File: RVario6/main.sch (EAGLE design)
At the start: 7 parts, among them J1 ZX62-B-5PA, U1 32U4

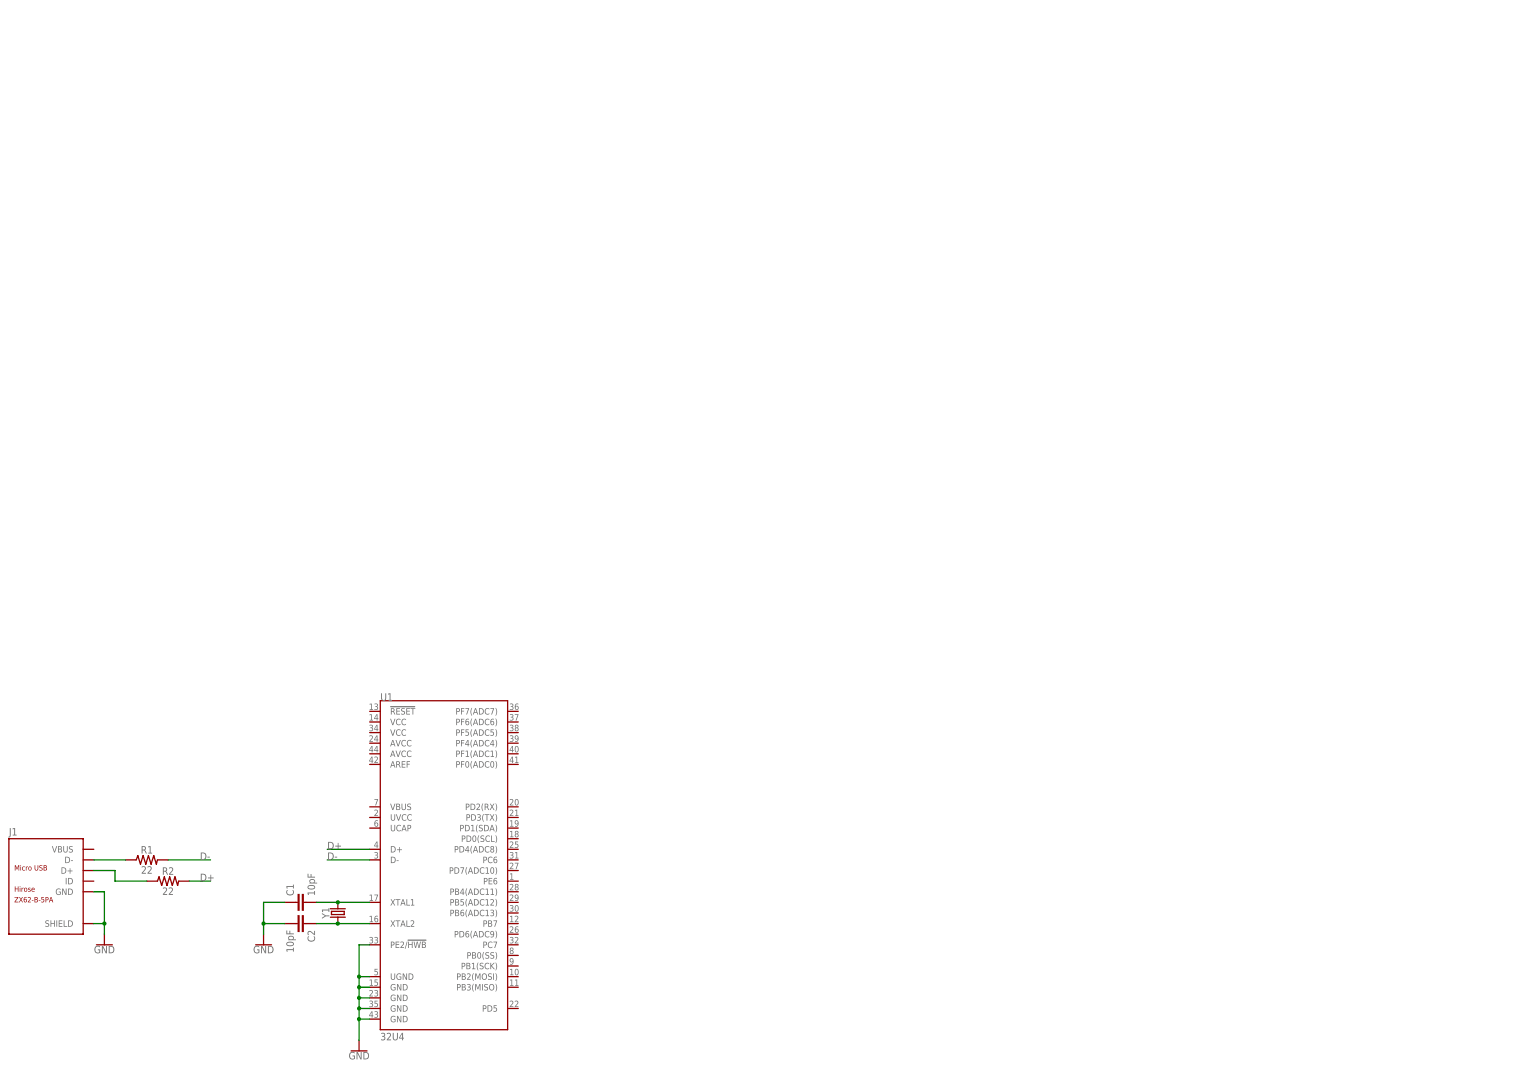
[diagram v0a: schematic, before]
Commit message: Finished schematic RVario6
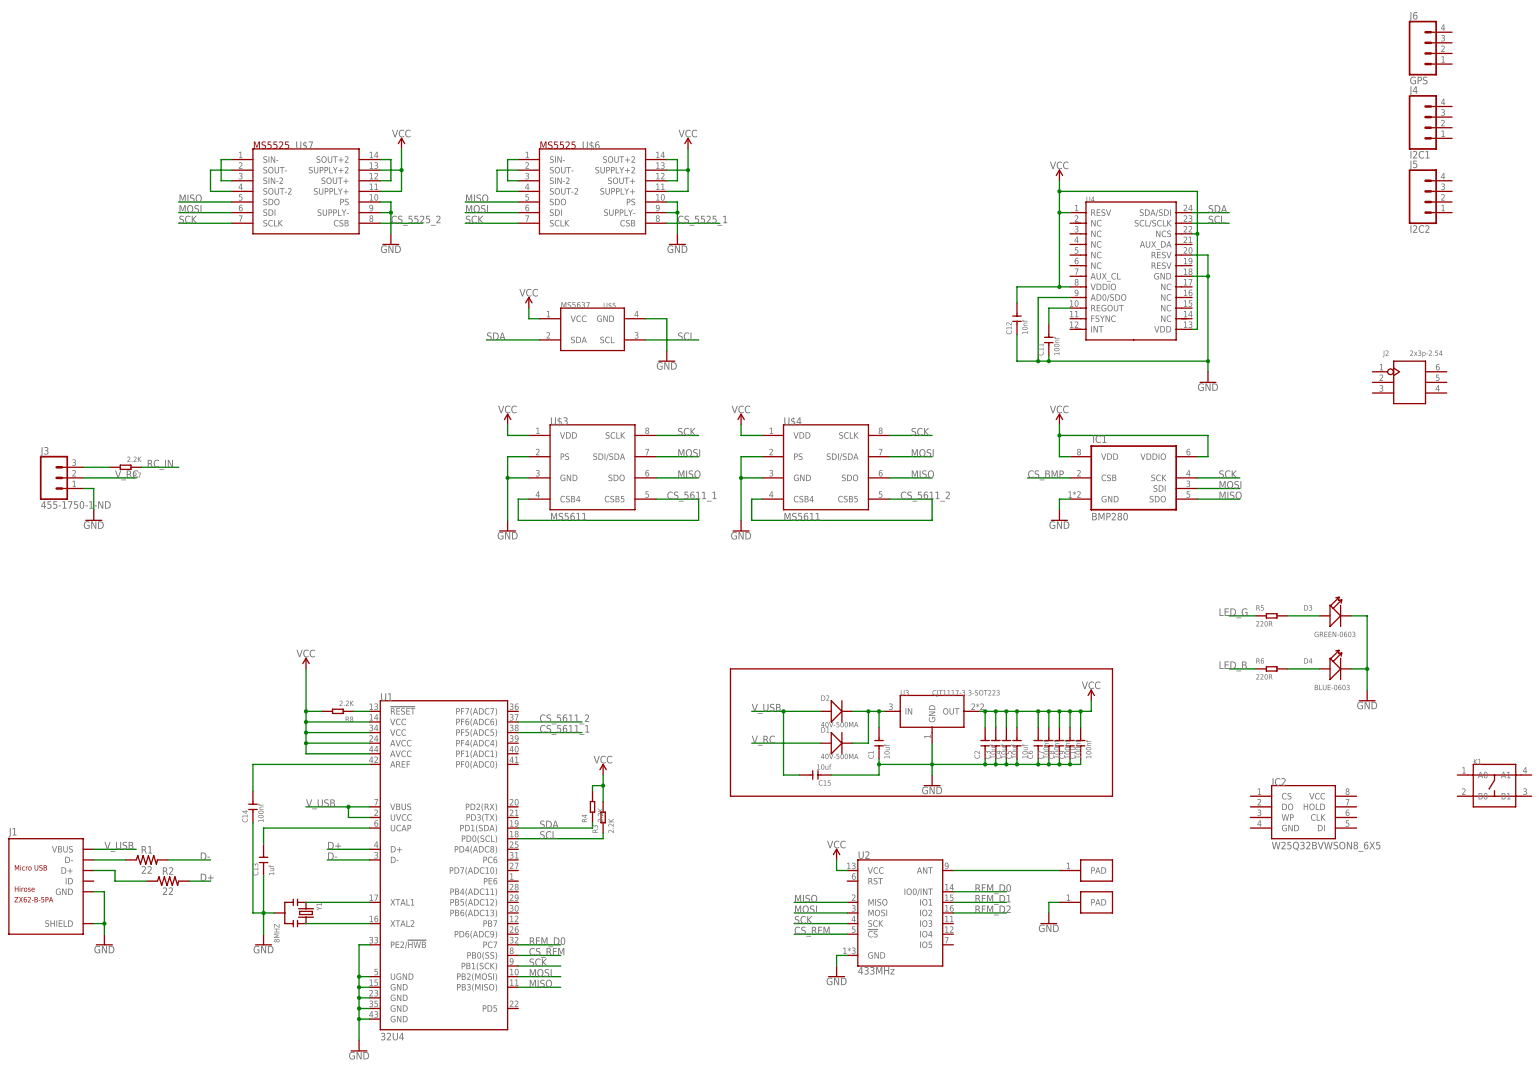
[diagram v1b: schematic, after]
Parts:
- added C10, C11, C14, C6, C7, C8, C9: 100nf, Seeed-Capacitor:CERAMIC-100NF-50V-10%-X7R(0603)
- added C12: 10nf, Seeed-Capacitor:CERAMIC-10NF-50V-10%-X7R(0603)
- added C13: 1uf, Seeed-Capacitor:CERAMIC-1UF-25V-10%-X7R(0603)
- added C15, C3, C4, C5: 10uf, Seeed-Capacitor:CERAMIC-10UF-25V-10%-X5R(0805)
- added D1, D2: 40V-500MA, Seeed-Diode:SMD-DIODE-SCHOTTKY-40V-500MA(SOD-123)
- added D3: GREEN-0603, Seeed-LED:SMD-LED-CLEAR-GREEN(0603)
- added D4: BLUE-0603, Seeed-LED:SMD-LED-CLEAR-BLUE(0603)
- added IC1: BMP280, bosch-bmp280:BMP280
- added IC2: W25Q32BVWSON8_6X5, Custom_old:W25Q32BVWSON8_6X5
- added J2: 2x3p-2.54, Seeed-Connector:DIP-BLACK-MALE-HEADER(2X3P-2.54）-2.54
- added J3: 455-1750-1-ND, SparkFun-Connectors:CONN_03
- added J4: I2C1, SparkFun-Connectors:CONN_04
- added J5: I2C2, SparkFun-Connectors:CONN_04
- added J6: GPS, SparkFun-Connectors:CONN_04
- added K1: (no value), Seeed-Switch:SMD-SWITCH-TACTILE-SPST-NO(4P-D6.0MM)
- added R3, R4, R7, R8: 2.2K, Seeed-Resistor:SMD-RES-2.2K-5%-1/10W(0603)
- added R5, R6: 220R, Seeed-Resistor:SMD-RES-220R-5%-1/10W(0603)
- added U$1, U$2: PADPAD_2.5X1.5, Custom_old:PADPAD_2.5X1.5
- added U$3, U$4: MS5611, Custom_old:MS5611
- added U$5: MS5637, Custom_old:MS5637
- added U$6, U$7: MS5525, Custom_old:MS5525
- added U2: 433MHz, SparkFun-RF:RFM69HCW-433
- added U3: CJT1117-3.3-SOT223, Seeed-IC:PMIC-CJT1117-3.3(SOT223)
- added U4: (no value), Seeed-Sensor:MOTION/POSITION-MPU-9250(QFN24G)
- C1, C2: value 10pF -> 10uf; device SparkFun-Capacitors:0.1UF-0603-25V-5% -> Seeed-Capacitor:CERAMIC-10UF-25V-10%-X5R(0805)
- Y1: value (none) -> 8MHZ; device SparkFun-Clocks:CRYSTALSMD-5X3.2-4PAD -> Seeed-Crystal Oscillator:SMD-CRYSTAL-8MHZ--0.3%-150R(3P-3.6X1.3MM)
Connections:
- new net CS_5525_1: U$6.CSB
- new net CS_5525_2: U$7.CSB
- new net CS_5611_1: U$3.CSB4, U$3.CSB5, U1.PF5(ADC5)
- new net CS_5611_2: U$4.CSB4, U$4.CSB5, U1.PF6(ADC6)
- new net CS_BMP: IC1.CSB
- new net CS_RFM: U1.PB0(SS), U2.!CS
- new net LED_B: R6.1
- new net LED_G: R5.1
- new net MISO: IC1.SDO, U$3.SDO, U$4.SDO, U$6.SDO, U$7.SDO, U1.PB3(MISO), U2.MISO
- new net MOSI: IC1.SDI, U$3.SDI/SDA, U$4.SDI/SDA, U$6.SDI, U$7.SDI, U1.PB2(MOSI), U2.MOSI
- new net N$10: C11.2, U4.REGOUT
- new net N$11: U$7.SIN-, U$7.SIN-2
- new net N$12: U$7.SOUT-, U$7.SOUT-2
- new net N$13: U$7.SOUT+, U$7.SOUT+2
- new net N$14: D3.+, R5.2
- new net N$15: D4.+, R6.2
- new net N$16: C13.2, U1.UCAP
- new net N$17: J3.3, R7.2
- new net N$18: R8.1, U1.!RESET
- new net N$19: C14.2, U1.AREF
- new net N$5: C1.2, D1.-, D2.-, U3.IN
- new net N$6: U$2.PAD, U2.ANT
- new net N$7: U$6.SIN-, U$6.SIN-2
- new net N$8: U$6.SOUT-, U$6.SOUT-2
- new net N$9: U$6.SOUT+, U$6.SOUT+2
- new net RC_IN: R7.1
- new net RFM_D0: U1.PC7, U2.IO0/INT
- new net RFM_D1: U2.IO1
- new net RFM_D2: U2.IO2
- new net SCK: IC1.SCK, U$3.SCLK, U$4.SCLK, U$6.SCLK, U$7.SCLK, U1.PB1(SCK), U2.SCK
- new net SCL: R3.1, U$5.SCL, U1.PD0(SCL), U4.SCL/SCLK
- new net SDA: R4.1, U$5.SDA, U1.PD1(SDA), U4.SDA/SDI
- new net VCC: C10.2, C12.2, C2.2, C3.2, C4.2, C5.2, C6.2, C7.2, C8.2, C9.2, IC1.VDD, IC1.VDDIO, R3.2, R4.2, R8.2, U$3.VDD, U$4.VDD, U$5.VCC, U$6.SUPPLY+, U$6.SUPPLY+2, U$7.SUPPLY+, U$7.SUPPLY+2, U1.AVCC@24, U1.AVCC@44, U1.VCC@14, U1.VCC@34, U2.VCC, U3.OUT, U4.NCS, U4.RESV, U4.VDD, U4.VDDIO
- new net V_RC: D1.+, J3.2
- new net V_USB: C15.2, D2.+, J1.VBUS, U1.UVCC, U1.VBUS
- net GND: now also C10.1, C11.1, C12.1, C13.1, C14.1, C15.1, C2.1, C3.1, C4.1, C5.1, C6.1, C7.1, C8.1, C9.1, D3.-, D4.-, IC1.GND, J3.1, U$1.PAD, U$3.GND, U$3.PS, U$4.GND, U$4.PS, U$5.GND, U$6.PS, U$6.SUPPLY-, U$7.PS, U$7.SUPPLY-, U2.GND, U3.GND, U4.AD0/SDO, U4.GND, U4.RESV@2, Y1.2; no longer C2.2
- net N$1: now also Y1.1; no longer C1.2, Y1.2
- net N$2: now also Y1.3; no longer C2.1, Y1.1

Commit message: Rvario6 updates
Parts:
- added J7: MICROSD-9P, Seeed-Connector:MICRO-SD-CARD-HOLDER-9P
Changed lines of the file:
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@@
 <part name="J6" library="SparkFun-Connectors" deviceset="CONN_04" device="" value="GPS"/>
 <part name="K1" library="Seeed-Switch" deviceset="SMD-SWITCH-TACTILE-SPST-NO(4P-D6.0MM)" device=""/>
+<part name="J7" library="Seeed-Connector" deviceset="MICRO-SD-CARD-HOLDER-9P" device="" value="MICROSD-9P"/>
 </parts>
 <sheets>
@@
 <instance part="J6" gate="G$1" x="342.9" y="269.24"/>
 <instance part="K1" gate="G$1" x="358.14" y="93.98"/>
+<instance part="J7" gate="G$1" x="391.16" y="157.48"/>
 </instances>
 <busses>

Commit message: Partiall routed
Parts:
- removed J5: I2C2, SparkFun-Connectors:CONN_04
- added C16, C17, C18: 100nf, Seeed-Capacitor:CERAMIC-100NF-50V-10%-X7R(0603)
- J4: value I2C1 -> GPS
- J6: value GPS -> I2C
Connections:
- net N$6 renamed ANT
- removed net N$18: R8.1, U1.!RESET
- new net BTN: K1.A0, U1.PD4(ADC8)
- new net CS_FLASH: IC2.CS, U1.PF7(ADC7)
- new net CS_SD: J7.CS, U1.PF4(ADC4)
- new net MRST: J4.2, U1.PD2(RX)
- new net MTSR: J4.1, U1.PD3(TX)
- new net RESET: J2.3, R8.1, U1.!RESET
- net CS_5525_1: now also U1.PC6
- net CS_5525_2: now also U1.PD7(ADC10)
- net CS_BMP: now also U1.PE6
- net GND: now also C16.1, C17.1, C18.1, IC2.GND, J2.4, J4.3, J6.1, J7.G1, J7.G2, J7.G3, J7.G4, J7.VSS, K1.B0, K1.B1
- net LED_B: now also U1.PF0(ADC0)
- net LED_G: now also U1.PF1(ADC1)
- net MISO: now also IC2.DO, J2.1, J7.DO
- net MOSI: now also IC2.DI, J2.5, J7.DI
- net RC_IN: now also U1.PB4(ADC11)
- net RFM_D1: now also U1.PB5(ADC12)
- net RFM_D2: now also U1.PB6(ADC13)
- net SCK: now also IC2.CLK, J2.2, J7.SCLK
- net SCL: now also J6.4
- net SDA: now also J6.3
- net VCC: now also C16.2, C17.2, C18.2, IC2.HOLD, IC2.VCC, IC2.WP, J2.6, J4.4, J6.2, J7.VDD
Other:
- moved on the sheet: IC2, J4, R8

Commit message: partially routed
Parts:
- removed J4: GPS, SparkFun-Connectors:CONN_04
- removed R7: 2.2K, Seeed-Resistor:SMD-RES-2.2K-5%-1/10W(0603)
- added Q1, Q2: CJ2302, Seeed-Transistor:SMD-MOSFET-N-CH-20V-2.1A-CJ2302(SOT-23)
- added R10, R9: 2.2K, Seeed-Resistor:SMD-RES-2.2K-5%-1/10W(0603)
- added R11: 47K, Seeed-Resistor:SMD-RES-47K-5%-1/10W(0603)
- J3: value 455-1750-1-ND -> (none)
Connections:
- removed net MRST: J4.2, U1.PD2(RX)
- removed net MTSR: J4.1, U1.PD3(TX)
- removed net N$17: J3.3, R7.2
- new net N$6: Q2.D, R10.1
- new net RX_INV: Q1.D, R9.1, U1.PD2(RX)
- new net TX_INV: Q2.G, U1.PD3(TX)
- net CS_BMP: now also U1.PF1(ADC1); no longer U1.PE6
- net GND: now also Q1.S, Q2.S; no longer J4.3
- net LED_G: now also U1.PE6; no longer U1.PF1(ADC1)
- net RC_IN: now also J3.3, Q1.G, R10.2, R11.1; no longer R7.1, U1.PB4(ADC11)
- net VCC: now also R11.2, R9.2; no longer J4.4
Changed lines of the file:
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@@
 <part name="GND14" library="SparkFun-PowerSymbols" deviceset="GND" device=""/>
 <part name="J2" library="Seeed-Connector" deviceset="DIP-BLACK-MALE-HEADER(2X3P-2.54）" device="-2.54" value="2x3p-2.54"/>
-<part name="J3" library="SparkFun-Connectors" deviceset="CONN_03" device="" value="455-1750-1-ND"/>
-<part name="GND15" library="SparkFun-PowerSymbols" deviceset="GND" device=""/>
-<part name="R7" library="Seeed-Resistor" deviceset="SMD-RES-2.2K-5%-1/10W(0603)" device="" value="2.2K"/>
+<part name="J3" library="SparkFun-Connectors" deviceset="CONN_03" device=""/>
 <part name="IC2" library="Custom_old" deviceset="W25Q32BV" device="WSON8_6X5" package3d_urn="urn:adsk.eagle:package:8074834/1" value=""/>
 <part name="C13" library="Seeed-Capacitor" deviceset="CERAMIC-1UF-25V-10%-X7R(0603)" device="" value="1uf"/>
@@
 <part name="SUPPLY14" library="SparkFun-PowerSymbols" deviceset="VCC" device=""/>
 <part name="GND19" library="SparkFun-PowerSymbols" deviceset="GND" device=""/>
-<part name="J4" library="SparkFun-Connectors" deviceset="CONN_04" device="" value="GPS"/>
 <part name="GND20" library="SparkFun-PowerSymbols" deviceset="GND" device=""/>
 <part name="SUPPLY15" library="SparkFun-PowerSymbols" deviceset="VCC" device=""/>
-<part name="GND21" library="SparkFun-PowerSymbols" deviceset="GND" device=""/>
-<part name="SUPPLY17" library="SparkFun-PowerSymbols" deviceset="VCC" device=""/>
 <part name="C16" library="Seeed-Capacitor" deviceset="CERAMIC-100NF-50V-10%-X7R(0603)" device="" value="100nf"/>
 <part name="C17" library="Seeed-Capacitor" deviceset="CERAMIC-100NF-50V-10%-X7R(0603)" device="" value="100nf"/>
 <part name="C18" library="Seeed-Capacitor" deviceset="CERAMIC-100NF-50V-10%-X7R(0603)" device="" value="100nf"/>
+<part name="Q1" library="Seeed-Transistor" deviceset="SMD-MOSFET-N-CH-20V-2.1A-CJ2302(SOT-23)" device="" value="CJ2302"/>
+<part name="Q2" library="Seeed-Transistor" deviceset="SMD-MOSFET-N-CH-20V-2.1A-CJ2302(SOT-23)" device="" value="CJ2302"/>
+<part name="R9" library="Seeed-Resistor" deviceset="SMD-RES-2.2K-5%-1/10W(0603)" device="" value="2.2K"/>
+<part name="R10" library="Seeed-Resistor" deviceset="SMD-RES-2.2K-5%-1/10W(0603)" device="" value="2.2K"/>
+<part name="R11" library="Seeed-Resistor" deviceset="SMD-RES-47K-5%-1/10W(0603)" device="" value="47K"/>
+<part name="SUPPLY16" library="SparkFun-PowerSymbols" deviceset="VCC" device=""/>
+<part name="GND22" library="SparkFun-PowerSymbols" deviceset="GND" device=""/>
 </parts>
 <sheets>
@@
 <instance part="J2" gate="J" x="337.82" y="190.5"/>
 <instance part="J3" gate="J$1" x="12.7" y="167.64"/>
-<instance part="GND15" gate="1" x="22.86" y="157.48"/>
-<instance part="R7" gate="G$1" x="30.48" y="170.18" rot="R180"/>
 <instance part="IC2" gate="G$1" x="312.42" y="66.04"/>
 <instance part="C13" gate="G$1" x="63.5" y="76.2" rot="R90"/>
@@
 <instance part="SUPPLY14" gate="G$1" x="347.98" y="195.58"/>
 <instance part="GND19" gate="1" x="347.98" y="182.88"/>
-<instance part="J4" gate="G$1" x="342.9" y="236.22"/>
 <instance part="GND20" gate="1" x="350.52" y="261.62"/>
 <instance part="SUPPLY15" gate="G$1" x="350.52" y="276.86"/>
-<instance part="GND21" gate="1" x="350.52" y="228.6"/>
-<instance part="SUPPLY17" gate="G$1" x="350.52" y="243.84"/>
 <instance part="C16" gate="G$1" x="261.62" y="104.14" rot="R90"/>
 <instance part="C17" gate="G$1" x="264.16" y="104.14" rot="R90"/>
 <instance part="C18" gate="G$1" x="266.7" y="104.14" rot="R90"/>
+<instance part="Q1" gate="G$1" x="53.34" y="170.18"/>
+<instance part="Q2" gate="G$1" x="45.72" y="154.94"/>
+<instance part="R9" gate="G$1" x="53.34" y="182.88" rot="R90"/>
+<instance part="R10" gate="G$1" x="45.72" y="165.1" rot="R90"/>
+<instance part="R11" gate="G$1" x="45.72" y="182.88" rot="R90"/>
+<instance part="SUPPLY16" gate="G$1" x="53.34" y="190.5"/>
+<instance part="GND22" gate="1" x="45.72" y="144.78"/>
 </instances>
 <busses>
@@
 </segment>
 <segment>
-<pinref part="J3" gate="J$1" pin="1"/>
-<pinref part="GND15" gate="1" pin="GND"/>
-<wire x1="20.32" y1="165.1" x2="22.86" y2="165.1" width="0.1524" layer="91"/>
-<wire x1="22.86" y1="165.1" x2="22.86" y2="160.02" width="0.1524" layer="91"/>
-</segment>
-<segment>
 <pinref part="K1" gate="G$1" pin="B1"/>
 <pinref part="GND16" gate="1" pin="GND"/>
@@
 </segment>
 <segment>
-<pinref part="J4" gate="G$1" pin="3"/>
-<pinref part="GND21" gate="1" pin="GND"/>
-<wire x1="347.98" y1="238.76" x2="350.52" y2="238.76" width="0.1524" layer="91"/>
-<wire x1="350.52" y1="238.76" x2="350.52" y2="231.14" width="0.1524" layer="91"/>
+<pinref part="J3" gate="J$1" pin="1"/>
+<wire x1="20.32" y1="165.1" x2="30.48" y2="165.1" width="0.1524" layer="91"/>
+<wire x1="30.48" y1="165.1" x2="30.48" y2="149.86" width="0.1524" layer="91"/>
+<pinref part="Q2" gate="G$1" pin="S"/>
+<wire x1="30.48" y1="149.86" x2="45.72" y2="149.86" width="0.1524" layer="91"/>
+<pinref part="GND22" gate="1" pin="GND"/>
+<wire x1="45.72" y1="147.32" x2="45.72" y2="149.86" width="0.1524" layer="91"/>
+<junction x="45.72" y="149.86"/>
+<pinref part="Q1" gate="G$1" pin="S"/>
+<wire x1="45.72" y1="149.86" x2="53.34" y2="149.86" width="0.1524" layer="91"/>
+<wire x1="53.34" y1="149.86" x2="53.34" y2="165.1" width="0.1524" layer="91"/>
 </segment>
 </net>
@@
 </segment>
 <segment>
-<pinref part="J4" gate="G$1" pin="4"/>
-<pinref part="SUPPLY17" gate="G$1" pin="VCC"/>
-<wire x1="347.98" y1="241.3" x2="350.52" y2="241.3" width="0.1524" layer="91"/>
-<wire x1="350.52" y1="241.3" x2="350.52" y2="243.84" width="0.1524" layer="91"/>
+<pinref part="R9" gate="G$1" pin="2"/>
+<pinref part="SUPPLY16" gate="G$1" pin="VCC"/>
+<wire x1="53.34" y1="186.69" x2="53.34" y2="187.96" width="0.1524" layer="91"/>
+<pinref part="R11" gate="G$1" pin="2"/>
+<wire x1="53.34" y1="187.96" x2="53.34" y2="190.5" width="0.1524" layer="91"/>
+<wire x1="45.72" y1="186.69" x2="45.72" y2="187.96" width="0.1524" layer="91"/>
+<wire x1="45.72" y1="187.96" x2="53.34" y2="187.96" width="0.1524" layer="91"/>
+<junction x="53.34" y="187.96"/>
 </segment>
 </net>
@@
 </segment>
 <segment>
-<pinref part="U1" gate="U1" pin="PE6"/>
-<wire x1="124.46" y1="71.12" x2="139.7" y2="71.12" width="0.1524" layer="91"/>
-<label x="129.54" y="71.12" size="1.778" layer="95"/>
+<pinref part="U1" gate="U1" pin="PF1(ADC1)"/>
+<wire x1="124.46" y1="101.6" x2="139.7" y2="101.6" width="0.1524" layer="91"/>
+<label x="129.54" y="101.6" size="1.778" layer="95"/>
 </segment>
 </net>
@@
 </segment>
 <segment>
-<pinref part="U1" gate="U1" pin="PF1(ADC1)"/>
-<wire x1="124.46" y1="101.6" x2="139.7" y2="101.6" width="0.1524" layer="91"/>
-<label x="129.54" y="101.6" size="1.778" layer="95"/>
+<pinref part="U1" gate="U1" pin="PE6"/>
+<wire x1="124.46" y1="71.12" x2="139.7" y2="71.12" width="0.1524" layer="91"/>
+<label x="129.54" y="71.12" size="1.778" layer="95"/>
 </segment>
 </net>
@@
 <segment>
 <pinref part="J3" gate="J$1" pin="2"/>
-<wire x1="20.32" y1="167.64" x2="33.02" y2="167.64" width="0.1524" layer="91"/>
-<label x="27.94" y="167.64" size="1.778" layer="95"/>
-</segment>
-</net>
-<net name="N$17" class="0">
-<segment>
+<wire x1="20.32" y1="167.64" x2="35.56" y2="167.64" width="0.1524" layer="91"/>
+<label x="30.48" y="167.64" size="1.778" layer="95"/>
+</segment>
+</net>
+<net name="RC_IN" class="0">
+<segment>
+<pinref part="Q1" gate="G$1" pin="G"/>
+<pinref part="R10" gate="G$1" pin="2"/>
+<wire x1="45.72" y1="170.18" x2="48.26" y2="170.18" width="0.1524" layer="91"/>
+<wire x1="45.72" y1="168.91" x2="45.72" y2="170.18" width="0.1524" layer="91"/>
+<junction x="45.72" y="170.18"/>
+<pinref part="R11" gate="G$1" pin="1"/>
+<wire x1="45.72" y1="179.07" x2="45.72" y2="170.18" width="0.1524" layer="91"/>
 <pinref part="J3" gate="J$1" pin="3"/>
-<wire x1="20.32" y1="170.18" x2="26.67" y2="170.18" width="0.1524" layer="91"/>
-<pinref part="R7" gate="G$1" pin="2"/>
-</segment>
-</net>
-<net name="RC_IN" class="0">
-<segment>
-<pinref part="R7" gate="G$1" pin="1"/>
-<wire x1="34.29" y1="170.18" x2="43.18" y2="170.18" width="0.1524" layer="91"/>
-<label x="35.56" y="170.18" size="1.778" layer="95"/>
-</segment>
-<segment>
-<pinref part="U1" gate="U1" pin="PB4(ADC11)"/>
-<wire x1="124.46" y1="68.58" x2="139.7" y2="68.58" width="0.1524" layer="91"/>
-<label x="129.54" y="68.58" size="1.778" layer="95"/>
+<wire x1="20.32" y1="170.18" x2="45.72" y2="170.18" width="0.1524" layer="91"/>
 </segment>
 </net>
@@
 </segment>
 </net>
-<net name="MRST" class="0">
-<segment>
-<pinref part="J4" gate="G$1" pin="2"/>
-<wire x1="347.98" y1="236.22" x2="365.76" y2="236.22" width="0.1524" layer="91"/>
-<label x="355.6" y="236.22" size="1.778" layer="95"/>
+<net name="N$6" class="0">
+<segment>
+<pinref part="R10" gate="G$1" pin="1"/>
+<pinref part="Q2" gate="G$1" pin="D"/>
+<wire x1="45.72" y1="161.29" x2="45.72" y2="160.02" width="0.1524" layer="91"/>
+</segment>
+</net>
+<net name="RX_INV" class="0">
+<segment>
+<pinref part="Q1" gate="G$1" pin="D"/>
+<pinref part="R9" gate="G$1" pin="1"/>
+<wire x1="53.34" y1="175.26" x2="53.34" y2="177.8" width="0.1524" layer="91"/>
+<wire x1="53.34" y1="177.8" x2="53.34" y2="179.07" width="0.1524" layer="91"/>
+<wire x1="53.34" y1="177.8" x2="60.96" y2="177.8" width="0.1524" layer="91"/>
+<junction x="53.34" y="177.8"/>
+<label x="58.42" y="177.8" size="1.778" layer="95"/>
 </segment>
 <segment>
@@
 </segment>
 </net>
-<net name="MTSR" class="0">
-<segment>
-<pinref part="J4" gate="G$1" pin="1"/>
-<wire x1="347.98" y1="233.68" x2="365.76" y2="233.68" width="0.1524" layer="91"/>
-<label x="355.6" y="233.68" size="1.778" layer="95"/>
-</segment>
-<segment>
+<net name="TX_INV" class="0">
+<segment>
+<pinref part="Q2" gate="G$1" pin="G"/>
+<wire x1="40.64" y1="154.94" x2="33.02" y2="154.94" width="0.1524" layer="91"/>
+<label x="33.02" y="154.94" size="1.778" layer="95"/>
+</segment>
+<segment>
